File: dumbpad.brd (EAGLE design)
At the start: 97 x 78.5 mm, 43 parts

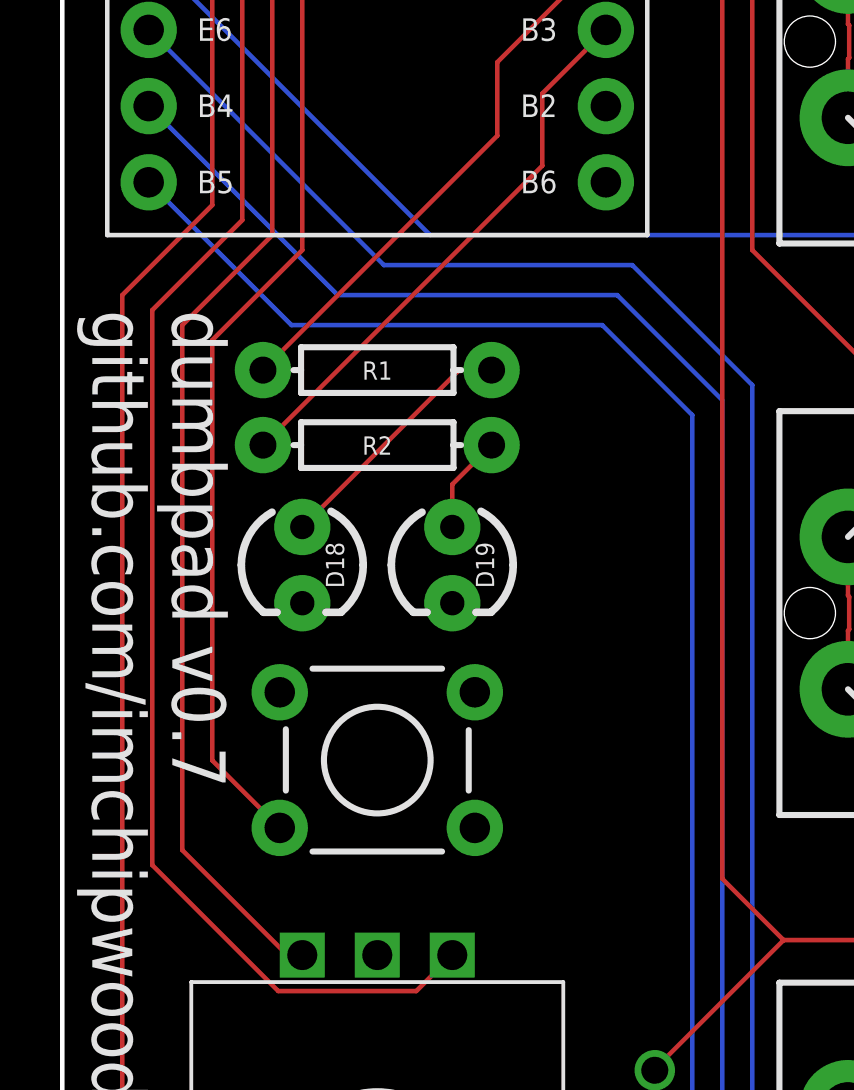
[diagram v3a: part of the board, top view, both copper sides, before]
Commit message: added 3rd LED for numlock indication
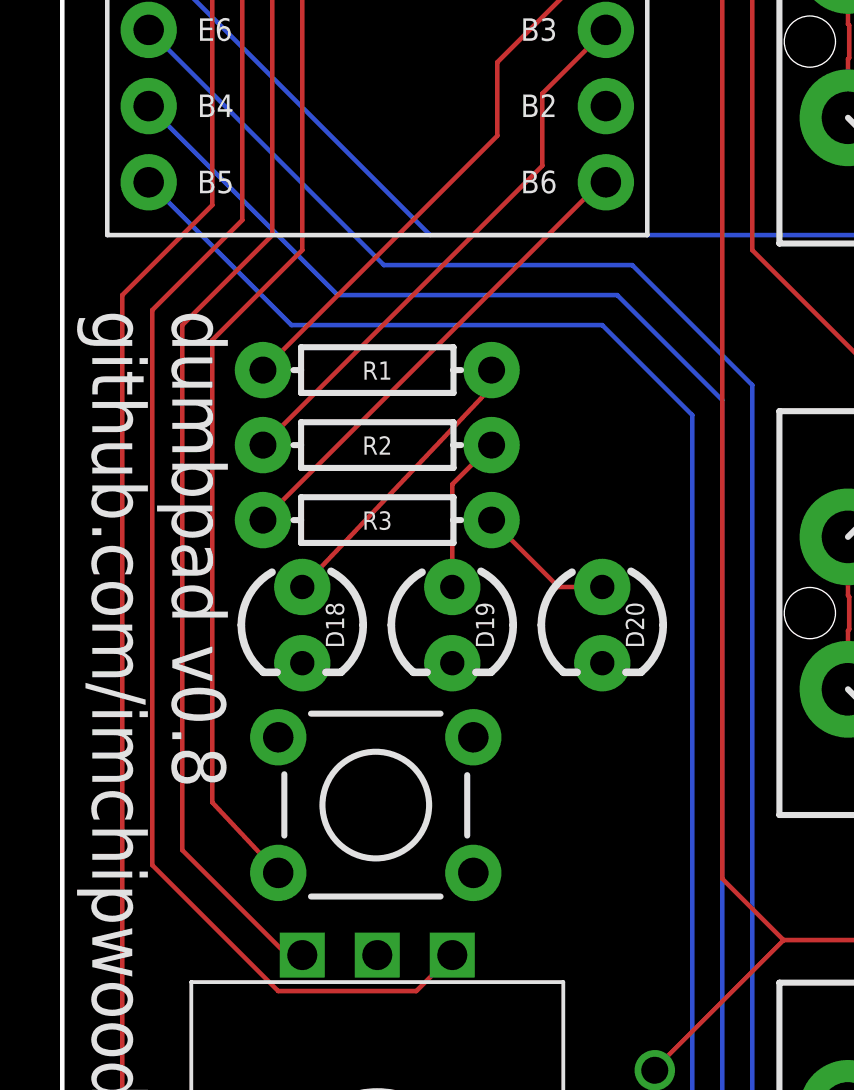
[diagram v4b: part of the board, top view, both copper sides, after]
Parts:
- added D20: (no value), SparkFun-LED:LED_3MM
- added R3: 330, SparkFun-Resistors:AXIAL-0.3
- moved D18 2.00 mm to (8.00, 29.5)
- moved D19 2.00 mm to (13.0, 29.5)
- moved S17 1.50 mm to (10.4, 23.5)
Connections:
- new net LED2: B1.13, R3.P$2
- new net N$10: D20.A, R3.P$1
- net GND: now also D20.K
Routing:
- net LED2: track 0.00 -> 16.1 mm
- net N$10: track 0.00 -> 4.61 mm
- net N$15: track 3.27 -> 5.27 mm
- net RESET: track 50.7 -> 52.2 mm
- net N$5: track 8.48 -> 9.74 mm
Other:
- board text added: "dumbpad v0.8 github.com/imchipwood"
- board text removed: "dumbpad v0.7 github.com/imchipwood"
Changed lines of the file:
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@@
 <board>
 <plain>
-<text x="1" y="40" size="1.778" layer="25" rot="SR270">dumbpad v0.7
+<text x="1" y="40" size="1.778" layer="25" rot="SR270">dumbpad v0.8
 github.com/imchipwood</text>
 <wire x1="1.5" y1="76" x2="6.5" y2="76" width="0.1524" layer="21"/>
@@
 <wire x1="14.5" y1="77.5" x2="14.5" y2="76" width="0.1524" layer="21"/>
 <text x="10.5" y="73.5" size="1.778" layer="21" align="bottom-center">pro micro</text>
-<text x="1" y="15" size="1.778" layer="26" rot="SMR90">dumbpad v0.7
+<text x="1" y="15" size="1.778" layer="26" rot="SMR90">dumbpad v0.8
 github.com/imchipwood</text>
 <text x="16.5" y="69.67" size="0.75" layer="21" align="center-right">GND</text>
@@
 </element>
 <element name="LOGO1" library="SparkFun-Aesthetics" package="OSHW-LOGO-L" value="OSHW-LOGOL" x="10.5" y="59.5" smashed="yes" rot="MR0"/>
-<element name="D18" library="SparkFun-LED" package="LED_3MM" value="" x="8" y="31.5" smashed="yes" rot="R270">
-<attribute name="NAME" x="8.786" y="31.5" size="0.6096" layer="25" font="vector" ratio="20" rot="R270" align="bottom-center"/>
-<attribute name="PROD_ID" value="DIO-08794" x="8" y="31.5" size="1.778" layer="27" rot="R270" display="off"/>
-<attribute name="VALUE" x="5.714" y="31.5" size="0.6096" layer="27" font="vector" ratio="20" rot="R270" align="top-center"/>
-</element>
-<element name="D19" library="SparkFun-LED" package="LED_3MM" value="" x="13" y="31.5" smashed="yes" rot="R270">
-<attribute name="NAME" x="13.786" y="31.5" size="0.6096" layer="25" font="vector" ratio="20" rot="R270" align="bottom-center"/>
-<attribute name="PROD_ID" value="DIO-08794" x="13" y="31.5" size="1.778" layer="27" rot="R270" display="off"/>
-<attribute name="VALUE" x="10.714" y="31.5" size="0.6096" layer="27" font="vector" ratio="20" rot="R270" align="top-center"/>
+<element name="D18" library="SparkFun-LED" package="LED_3MM" value="" x="8" y="29.5" smashed="yes" rot="R270">
+<attribute name="NAME" x="8.786" y="29.5" size="0.6096" layer="25" font="vector" ratio="20" rot="R270" align="bottom-center"/>
+<attribute name="PROD_ID" value="DIO-08794" x="8" y="29.5" size="1.778" layer="27" rot="R270" display="off"/>
+<attribute name="VALUE" x="5.714" y="29.5" size="0.6096" layer="27" font="vector" ratio="20" rot="R270" align="top-center"/>
+</element>
+<element name="D19" library="SparkFun-LED" package="LED_3MM" value="" x="13" y="29.5" smashed="yes" rot="R270">
+<attribute name="NAME" x="13.786" y="29.5" size="0.6096" layer="25" font="vector" ratio="20" rot="R270" align="bottom-center"/>
+<attribute name="PROD_ID" value="DIO-08794" x="13" y="29.5" size="1.778" layer="27" rot="R270" display="off"/>
+<attribute name="VALUE" x="10.714" y="29.5" size="0.6096" layer="27" font="vector" ratio="20" rot="R270" align="top-center"/>
 </element>
 <element name="R1" library="SparkFun-Resistors" package="AXIAL-0.3" value="330" x="10.5" y="38" smashed="yes" rot="R180">
@@
 <attribute name="PROD_ID" value="RES-8371" x="10.5" y="35.5" size="1.778" layer="27" rot="R180" display="off"/>
 </element>
-<element name="S17" library="SparkFun-Switches" package="TACTILE_SWITCH_PTH_6.0MM" value="MOMENTARY-SWITCH-SPST-PTH-6.0MM" x="10.5" y="25" smashed="yes">
-<attribute name="PROD_ID" value=" SWCH-08441" x="10.5" y="25" size="1.778" layer="27" display="off"/>
-<attribute name="SF_SKU" value="COM-00097" x="10.5" y="25" size="1.778" layer="27" display="off"/>
+<element name="S17" library="SparkFun-Switches" package="TACTILE_SWITCH_PTH_6.0MM" value="MOMENTARY-SWITCH-SPST-PTH-6.0MM" x="10.45" y="23.5" smashed="yes">
+<attribute name="PROD_ID" value=" SWCH-08441" x="10.45" y="23.5" size="1.778" layer="27" display="off"/>
+<attribute name="SF_SKU" value="COM-00097" x="10.45" y="23.5" size="1.778" layer="27" display="off"/>
 </element>
 <element name="JP1" library="SparkFun-Jumpers" package="SMT-JUMPER_3_NO_NO-SILK" value="JUMPER-SMT_3_NO_NO-SILK" x="19.75" y="4.95" smashed="yes" rot="R180"/>
 <element name="JP2" library="SparkFun-Jumpers" package="SMT-JUMPER_3_NO_NO-SILK" value="JUMPER-SMT_3_NO_NO-SILK" x="2" y="4.95" smashed="yes" rot="R180"/>
+<element name="D20" library="SparkFun-LED" package="LED_3MM" value="" x="18" y="29.5" smashed="yes" rot="R270">
+<attribute name="NAME" x="18.786" y="29.5" size="0.6096" layer="25" font="vector" ratio="20" rot="R270" align="bottom-center"/>
+<attribute name="PROD_ID" value="DIO-08794" x="18" y="29.5" size="1.778" layer="27" rot="R270" display="off"/>
+<attribute name="VALUE" x="15.714" y="29.5" size="0.6096" layer="27" font="vector" ratio="20" rot="R270" align="top-center"/>
+</element>
+<element name="R3" library="SparkFun-Resistors" package="AXIAL-0.3" value="330" x="10.5" y="33" smashed="yes" rot="R180">
+<attribute name="NAME" x="10.5" y="32.984" size="0.6096" layer="25" font="vector" ratio="20" rot="R180" align="center"/>
+<attribute name="PROD_ID" value="RES-8371" x="10.5" y="33" size="1.778" layer="27" rot="R180" display="off"/>
+<attribute name="VALUE" x="10.5" y="34.016" size="0.6096" layer="27" font="vector" ratio="20" rot="R180" align="top-center"/>
+</element>
 </elements>
 <signals>
@@
 <contactref element="D19" pad="K"/>
 <contactref element="S17" pad="1"/>
+<contactref element="D20" pad="K"/>
 </signal>
 <signal name="RAW">
@@
 <wire x1="8" y1="42" x2="5" y2="39" width="0.1524" layer="1"/>
 <wire x1="8" y1="42" x2="8" y2="57" width="0.1524" layer="1"/>
-<wire x1="5" y1="24.9882" x2="7.2488" y2="22.7394" width="0.1524" layer="1"/>
-<wire x1="5" y1="39" x2="5" y2="24.9882" width="0.1524" layer="1"/>
+<wire x1="5" y1="23.5882" x2="7.1988" y2="21.2394" width="0.1524" layer="1"/>
+<wire x1="5" y1="39" x2="5" y2="23.5882" width="0.1524" layer="1"/>
 </signal>
 <signal name="COL4">
@@
 <contactref element="D18" pad="A"/>
 <contactref element="R1" pad="P$1"/>
-<wire x1="8" y1="32.77" x2="13.23" y2="38" width="0.1524" layer="1"/>
-<wire x1="13.23" y1="38" x2="14.31" y2="38" width="0.1524" layer="1"/>
+<wire x1="14.31" y1="38" x2="14.31" y2="37.43" width="0.1524" layer="1"/>
+<wire x1="14.31" y1="37.43" x2="8" y2="30.77" width="0.1524" layer="1"/>
 </signal>
 <signal name="N$15">
 <contactref element="R2" pad="P$1"/>
 <contactref element="D19" pad="A"/>
-<wire x1="13" y1="32.77" x2="13" y2="34.19" width="0.1524" layer="1"/>
+<wire x1="13" y1="30.77" x2="13" y2="34.19" width="0.1524" layer="1"/>
 <wire x1="13" y1="34.19" x2="14.31" y2="35.5" width="0.1524" layer="1"/>
 </signal>
@@
 <wire x1="19.75" y1="7.04" x2="19.75" y2="4.95" width="0.1524" layer="1"/>
 </signal>
+<signal name="LED2">
+<contactref element="B1" pad="13"/>
+<contactref element="R3" pad="P$2"/>
+<wire x1="6.69" y1="33" x2="17.95" y2="44.26" width="0.1524" layer="1"/>
+<wire x1="17.95" y1="44.26" x2="18.12" y2="44.26" width="0.1524" layer="1"/>
+</signal>
+<signal name="N$10">
+<contactref element="D20" pad="A"/>
+<contactref element="R3" pad="P$1"/>
+<wire x1="18" y1="30.77" x2="16.54" y2="30.77" width="0.1524" layer="1"/>
+<wire x1="16.54" y1="30.77" x2="14.31" y2="33" width="0.1524" layer="1"/>
+</signal>
 </signals>

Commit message: moved LEDs, added more gs
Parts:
- added LOGO2: OSHW-LOGOL, SparkFun-Aesthetics:OSHW-LOGO-L
- moved D18 2.50 mm to (5.50, 29.4)
- moved D19 2.50 mm to (10.5, 29.4)
- moved D20 2.50 mm to (15.5, 29.4)
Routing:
- net N$5: track 9.74 -> 11.8 mm
- net N$10: track 4.61 -> 2.82 mm
- net N$15: track 5.27 -> 6.41 mm
- net ENCODER_L1: track 45.9 -> 46.8 mm
- net ENCODER_L0: track 50.2 -> 51.1 mm
- net COL0: track 51.6 -> 52.4 mm
- net RESET: track 52.2 -> 53.0 mm
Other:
- board text added: "dumbpad v0.8"
- board text added: "github.com/imchipwood"
- board text removed: "dumbpad v0.8 github.com/imchipwood"
